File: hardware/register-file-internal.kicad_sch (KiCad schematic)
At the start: 6 parts, among them U12 74AHC373, U14 74AHC373, U2 74AHC04

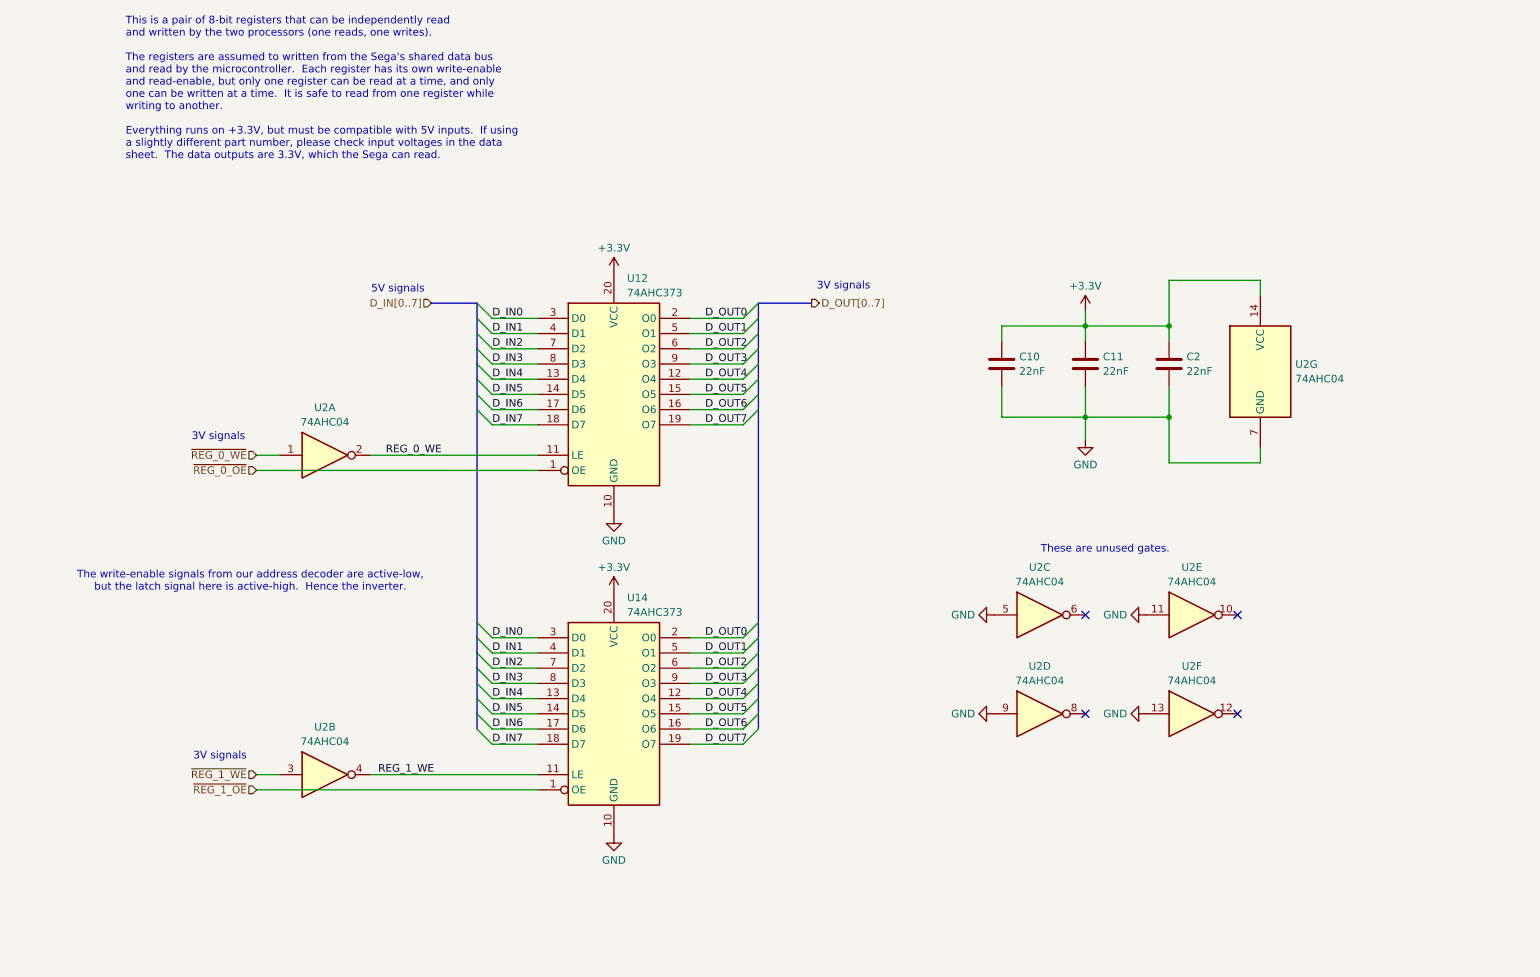
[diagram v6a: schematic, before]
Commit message: Move microcontroller board design into shareable subsheet
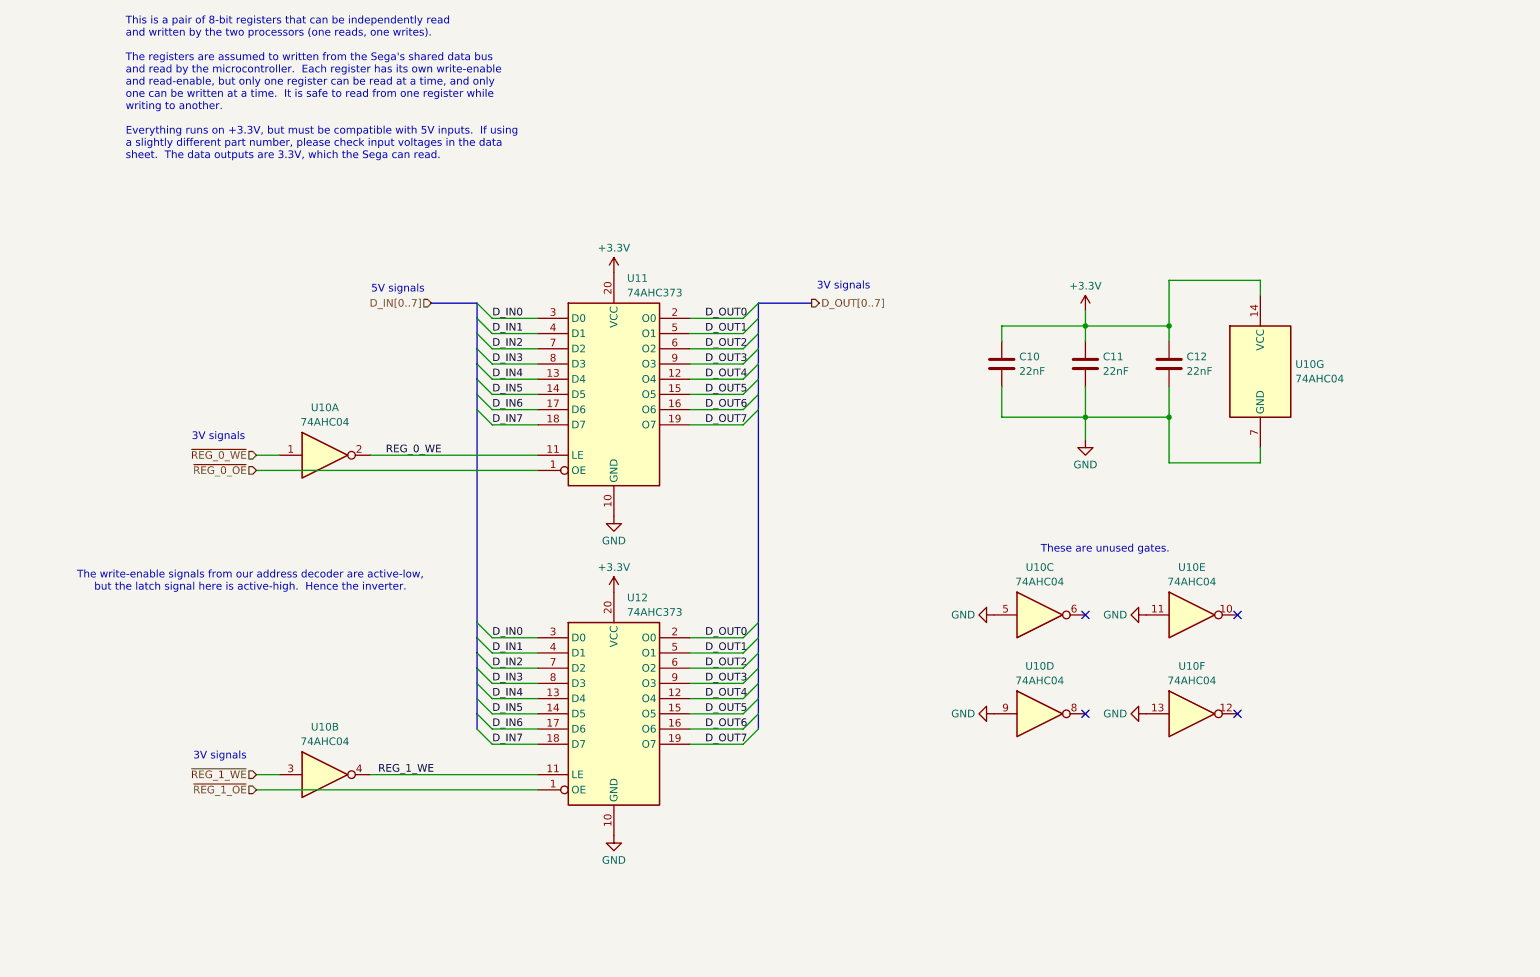
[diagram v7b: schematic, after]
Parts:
- renumbered C2 to C12, U2 to U10, U12 to U11, U14 to U12

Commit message: Reannotate schematics and drop debug bridges
Parts are now numbered starting at 0 for cart, 100 for SRAM, 300 for
microcontroller.

Also, drop debug bridges that made routing more difficult and had the
same names across prototype boards.

Hopefully this will help avoid naming conflicts for the unified PCB.

Also, redo prototype PCB layouts.

Now that all the names have changed, update board layouts.
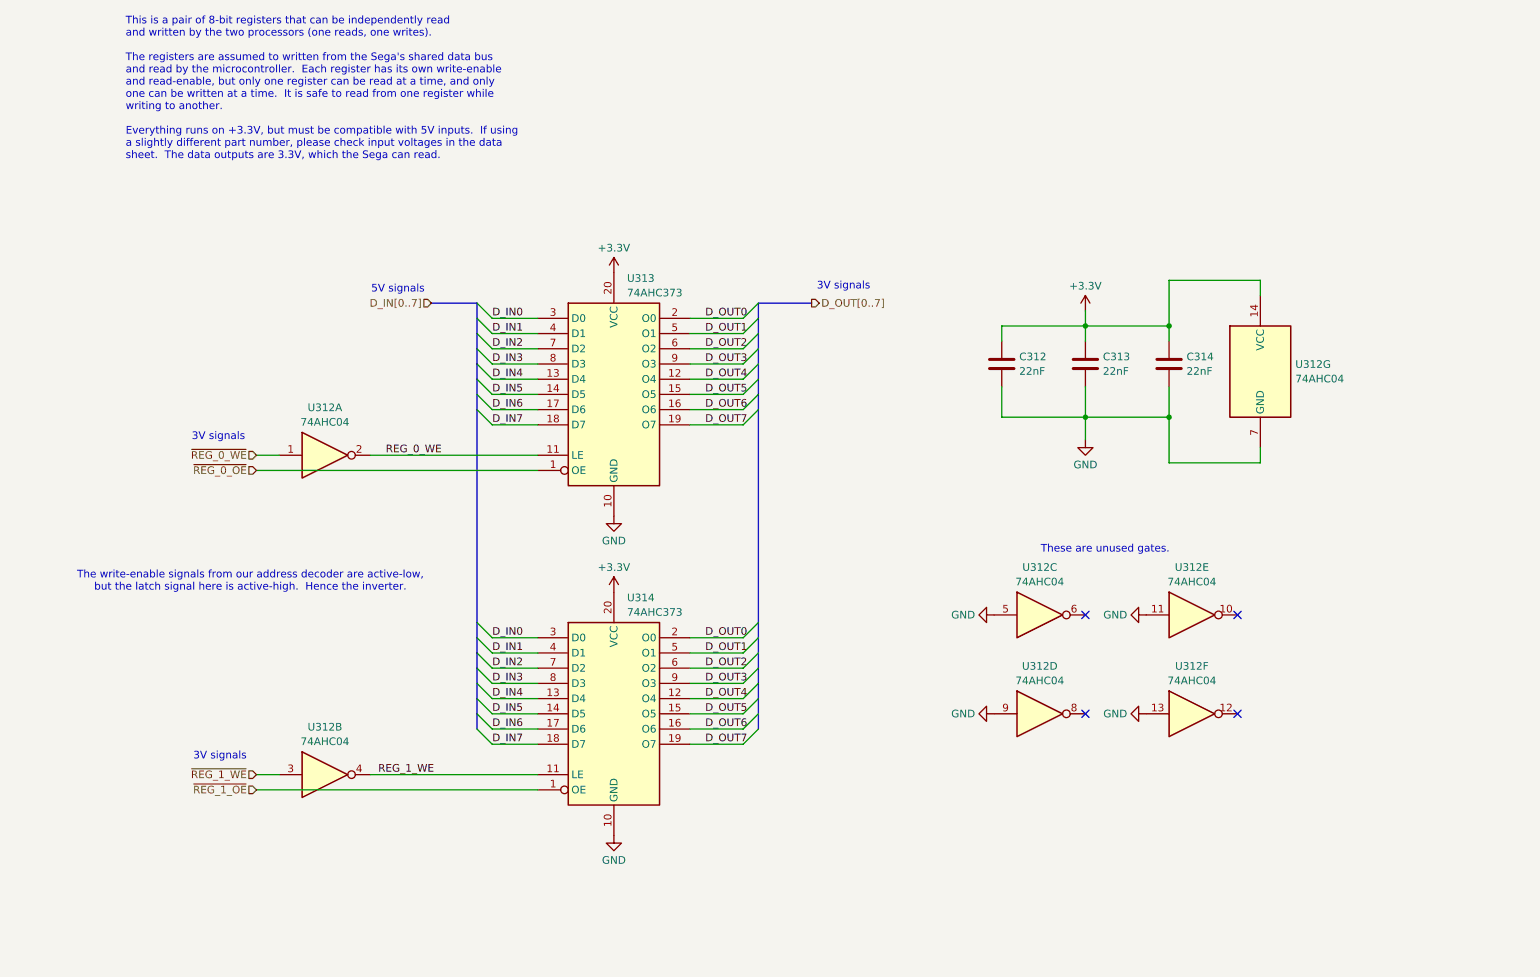
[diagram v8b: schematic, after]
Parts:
- renumbered C10 to C312, C11 to C313, C12 to C314, U10 to U312, U11 to U313, U12 to U314
